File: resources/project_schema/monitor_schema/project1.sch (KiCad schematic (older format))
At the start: 11 parts, among them J1 Conn_01x04, J2 Conn_01x06, SW1 SW_DPST_x2, U1 ESP32-WROOM

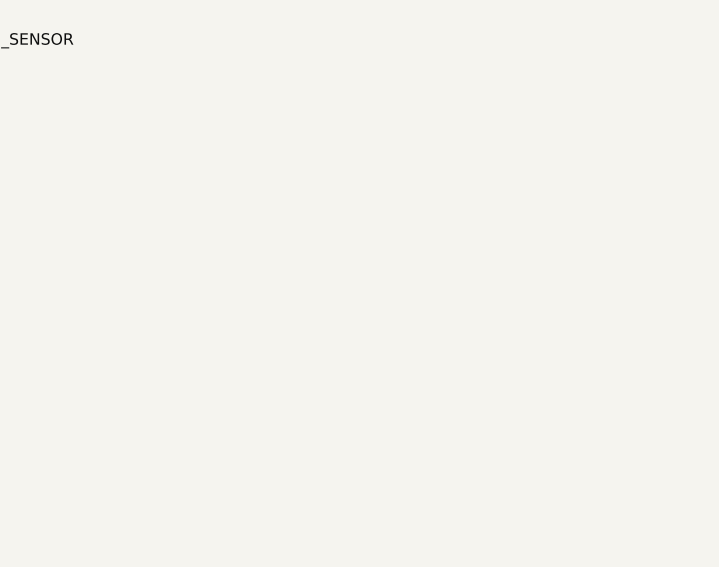
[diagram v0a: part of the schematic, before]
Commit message: add esp32 schema kicad
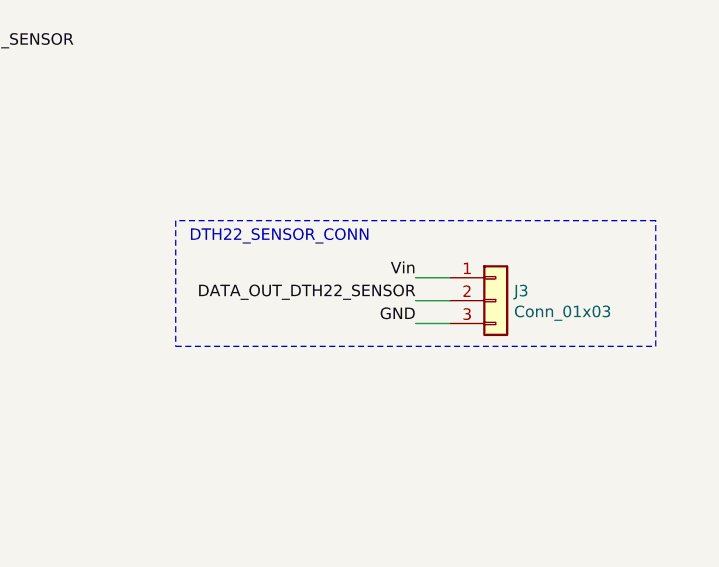
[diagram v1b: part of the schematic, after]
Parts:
- added J3: Conn_01x03, symbol Connector_Generic:Conn_01x03
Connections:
- net +3V3: now also J3.1 (Pin_1)
- net DATA_OUT_DTH22_SENSOR: now also J3.2 (Pin_2)
- net GND: now also J3.3 (Pin_3)
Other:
- note added: "DTH22_SENSOR_CONN"
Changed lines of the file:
@@
 $EndDescr
-$Comp
-L esp32v2:ESP32-WROOM U1
-U 1 1 61DCFA75
-P 6050 3850
-F 0 "U1" H 6025 5237 60  0000 C CNN
-F 1 "ESP32-WROOM" H 6025 5131 60  0000 C CNN
-F 2 "ESP32-footprints-Lib:ESP32-WROOM" H 6400 5200 60  0001 C CNN
-F 3 "" H 5600 4300 60  0001 C CNN
-	1    6050 3850
-	1    0    0    -1
-$EndComp
 $Comp
 L Device:R_US R2
@@
 Text Notes 9900 2800 2    50   ~ 0
 SD_INTERFACE
+$Comp
+L Connector_Generic:Conn_01x03 J3
+U 1 1 61DF05AB
+P 9950 5300
+F 0 "J3" H 10030 5342 50  0000 L CNN
+F 1 "Conn_01x03" H 10030 5251 50  0000 L CNN
+F 2 "" H 9950 5300 50  0001 C CNN
+F 3 "~" H 9950 5300 50  0001 C CNN
+	1    9950 5300
+	1    0    0    -1
+$EndComp
+Wire Wire Line
+	9750 5200 9600 5200
+Wire Wire Line
+	9750 5300 9600 5300
+Wire Wire Line
+	9750 5400 9600 5400
+Text Label 9600 5200 2    50   ~ 0
+Vin
+Text Label 9600 5300 2    50   ~ 0
+DATA_OUT_DTH22_SENSOR
+Text Label 9600 5400 2    50   ~ 0
+GND
+Wire Notes Line style solid
+	8550 4950 8550 5500
+Wire Notes Line style solid
+	8550 5500 10650 5500
+Wire Notes Line style solid
+	10650 5500 10650 4950
+Wire Notes Line style solid
+	10650 4950 8550 4950
+$Comp
+L esp32v2:ESP32-WROOM U1
+U 1 1 61DF6B71
+P 6050 3850
+F 0 "U1" H 6025 5237 60  0000 C CNN
+F 1 "ESP32-WROOM" H 6025 5131 60  0000 C CNN
+F 2 "ESP32-footprints-Lib:ESP32-WROOM" H 6400 5200 60  0001 C CNN
+F 3 "" H 5600 4300 60  0001 C CNN
+	1    6050 3850
+	1    0    0    -1
+$EndComp
+Text Notes 9400 5050 2    50   ~ 0
+DTH22_SENSOR_CONN
 $EndSCHEMATC

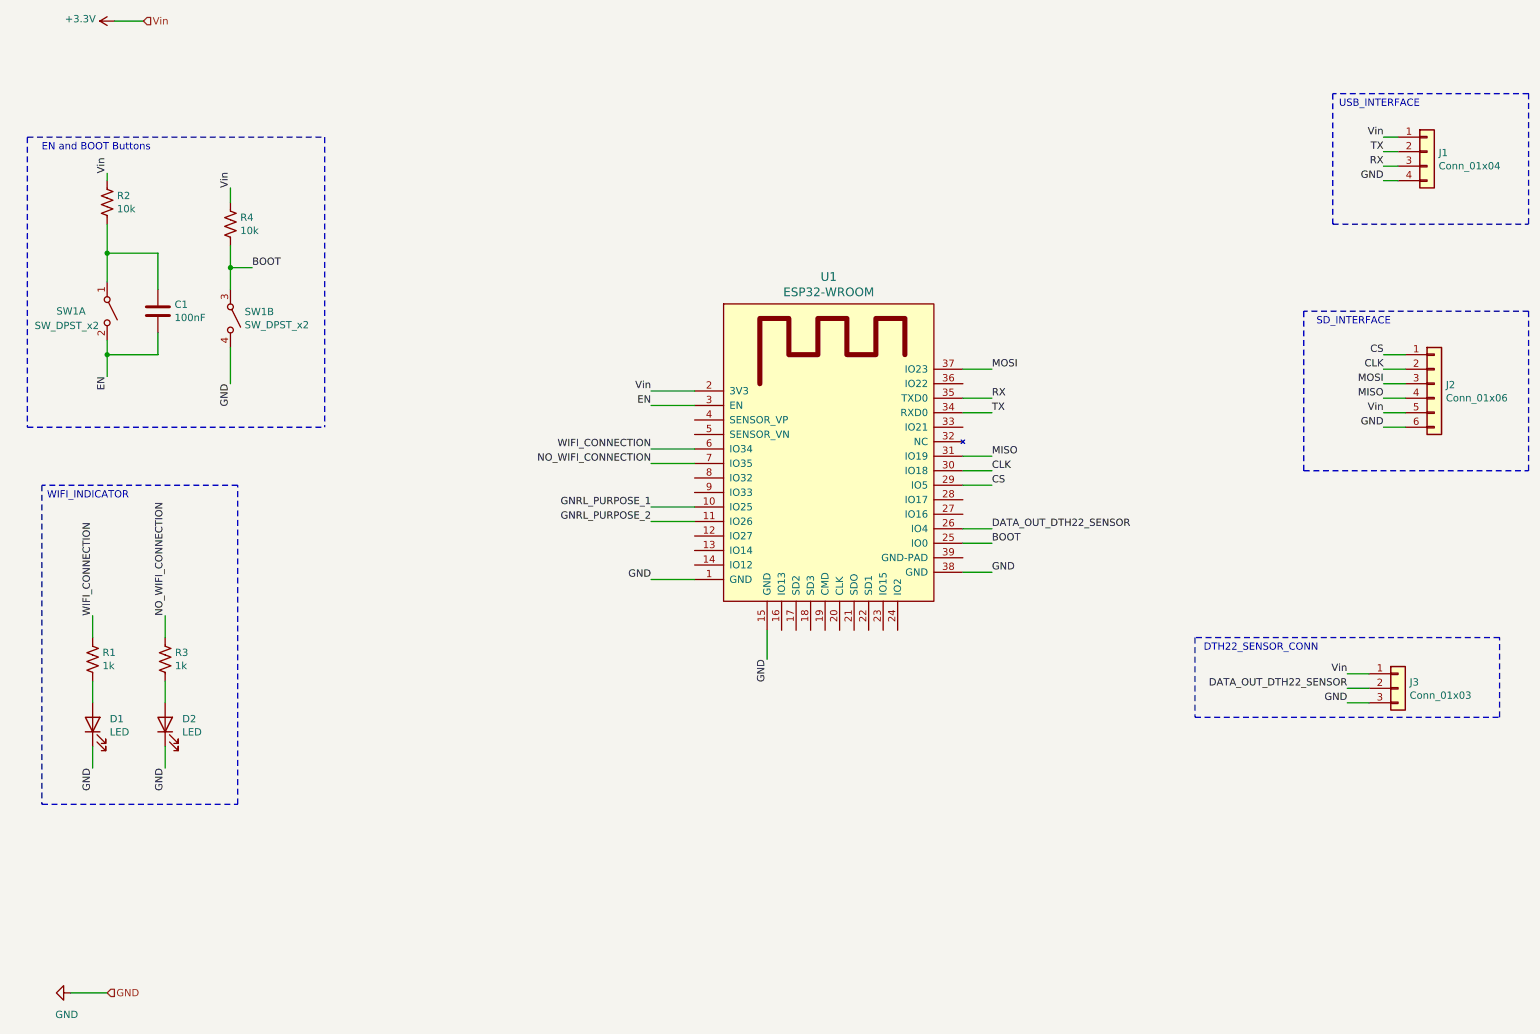
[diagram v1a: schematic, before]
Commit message: add pwr batt sensor and pwr regulator
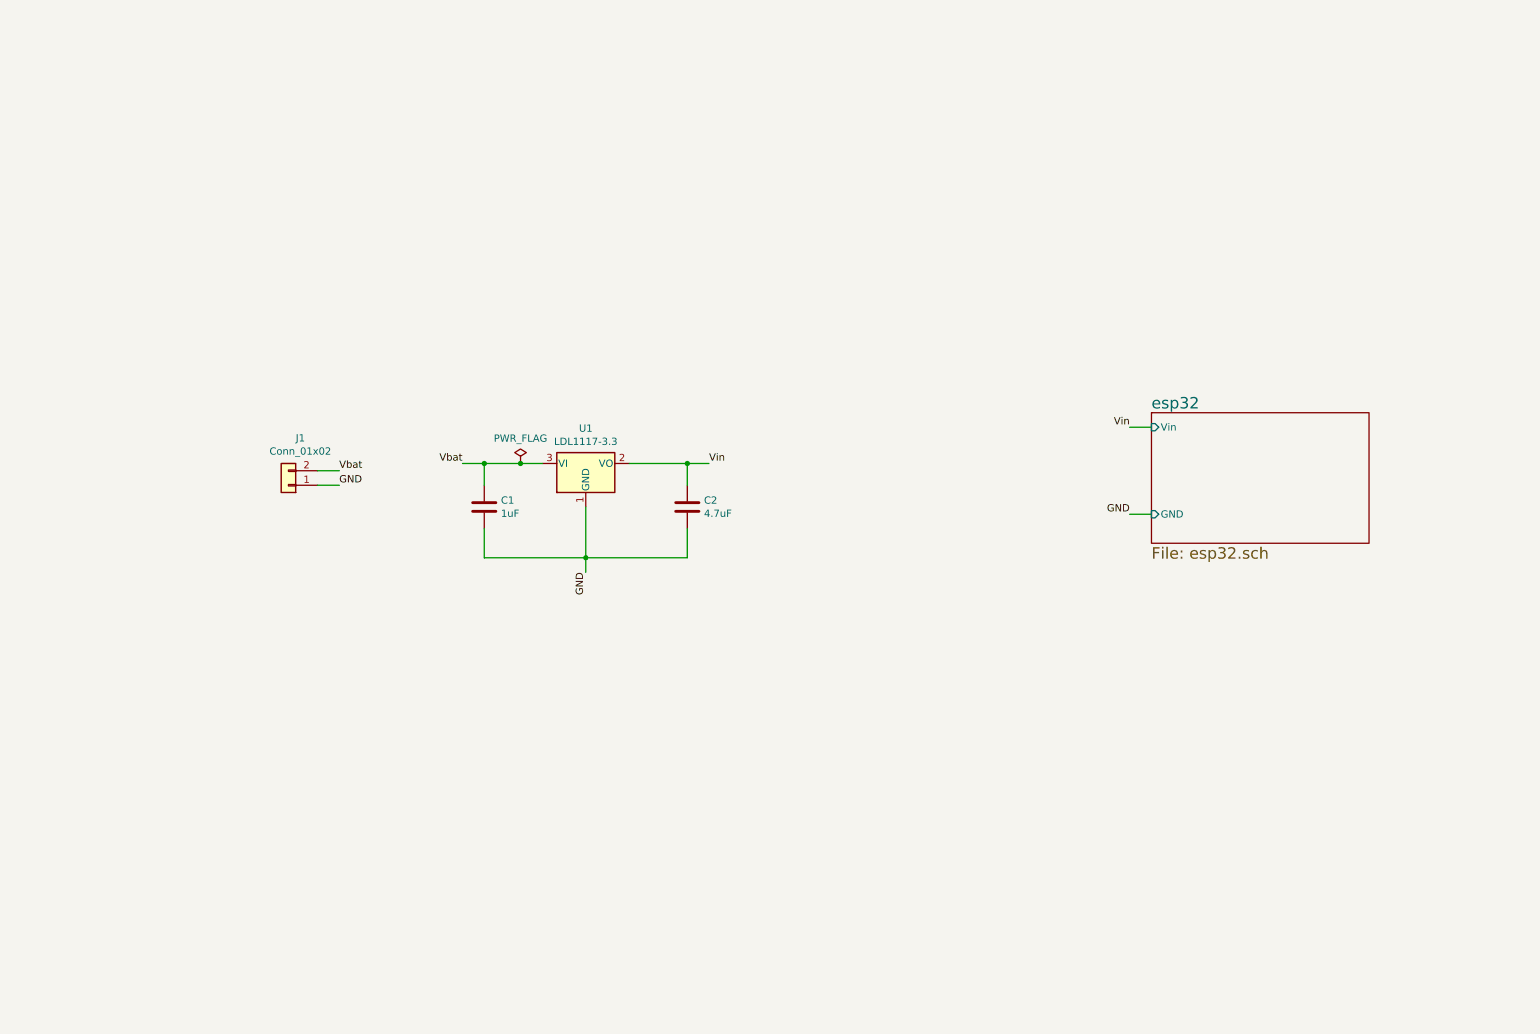
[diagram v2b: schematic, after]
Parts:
- removed D1, D2: LED, symbol Device:LED
- removed J1: Conn_01x04, symbol Connector_Generic:Conn_01x04
- removed J2: Conn_01x06, symbol Connector_Generic:Conn_01x06
- removed J3: Conn_01x03, symbol Connector_Generic:Conn_01x03
- removed R1, R3: 1k, symbol Device:R_US
- removed R2, R4: 10k, symbol Device:R_US
- removed SW1: SW_DPST_x2, symbol Switch:SW_DPST_x2
- removed U1: ESP32-WROOM, ESP32-footprints-Lib:ESP32-WROOM, symbol esp32v2:ESP32-WROOM
- added C2: 4.7uF, symbol Device:C
- added J1: Conn_01x02, symbol Connector_Generic:Conn_01x02
- added U1: LDL1117-3.3, Package_TO_SOT_SMD:SOT-223-3_TabPin2, symbol Regulator_Linear:AMS1117-3.3
- C1: value 100nF -> 1uF
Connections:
- net GND: now also C1.2, C2.2, J1.1 (Pin_1), U1.1 (GND)
- net EN renamed Vbat
- net Vbat: now also J1.2 (Pin_2), U1.3 (VI)
- new net Vin: C2.1, U1.2 (VO)
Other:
- note removed: "DTH22_SENSOR_CONN"
- note removed: "EN and BOOT Buttons"
- note removed: "SD_INTERFACE"
- note removed: "USB_INTERFACE"
- note removed: "WIFI_INDICATOR"

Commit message: Update pcb layout
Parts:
- C1, C2: footprint (none) -> Capacitor_SMD:C_0805_2012Metric_Pad1.18x1.45mm_HandSolder
- J1: footprint (none) -> Connector_PinHeader_2.54mm:PinHeader_1x02_P2.54mm_Vertical
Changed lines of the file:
@@
 F 0 "C2" H 5165 4096 50  0000 L CNN
 F 1 "4.7uF" H 5165 4005 50  0000 L CNN
-F 2 "" H 5088 3900 50  0001 C CNN
+F 2 "Capacitor_SMD:C_0805_2012Metric_Pad1.18x1.45mm_HandSolder" H 5088 3900 50  0001 C CNN
 F 3 "~" H 5050 4050 50  0001 C CNN
 	1    5050 4050
@@
 F 0 "C1" H 3765 4096 50  0000 L CNN
 F 1 "1uF" H 3765 4005 50  0000 L CNN
-F 2 "" H 3688 3900 50  0001 C CNN
+F 2 "Capacitor_SMD:C_0805_2012Metric_Pad1.18x1.45mm_HandSolder" H 3688 3900 50  0001 C CNN
 F 3 "~" H 3650 4050 50  0001 C CNN
 	1    3650 4050
@@
 F 0 "J1" H 2218 3575 50  0000 C CNN
 F 1 "Conn_01x02" H 2218 3666 50  0000 C CNN
-F 2 "" H 2300 3900 50  0001 C CNN
+F 2 "Connector_PinHeader_2.54mm:PinHeader_1x02_P2.54mm_Vertical" H 2300 3900 50  0001 C CNN
 F 3 "~" H 2300 3900 50  0001 C CNN
 	1    2300 3900
